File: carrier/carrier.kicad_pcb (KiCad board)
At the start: 4 copper layers, 10.2 x 7.6 mm, 2 parts, among them J1 DF40TC-30DP-0.4V(51), U1 HOME_VFBGA67_INTERFACE

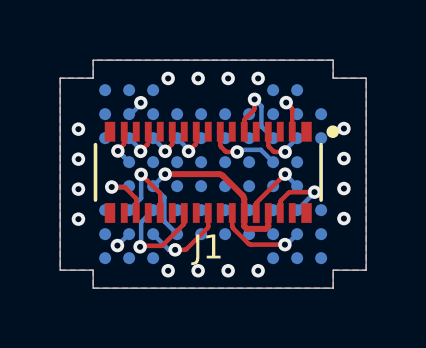
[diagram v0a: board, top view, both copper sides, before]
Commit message: Commit routed pinout, checkers, docs and mechanical outputs
Brings the repository up to the state that has been on disk and passing
`make check`: the routed same-number DF40 table replacing the old Courk
DF17-derived pinout, the mating and panel checkers, corrected connector
documentation, JLC rule tooling, and the 3D/mechanical outputs.

Committed as one baseline so the board C and board D work that follows has
reviewable per-task diffs.

Co-Authored-By: Claude Opus 5 <noreply@anthropic.com>
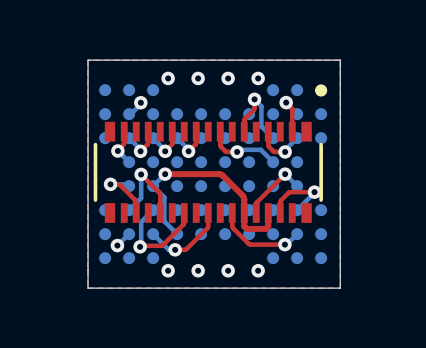
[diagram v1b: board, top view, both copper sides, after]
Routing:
- net GND: vias 18 -> 10
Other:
- board size 10.2 x 7.6 mm -> 8.4 x 7.6 mm
